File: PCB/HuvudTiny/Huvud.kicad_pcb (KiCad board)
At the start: 4 copper layers, 42 x 42 mm, 98 parts, among them J10 JST_PH, J12 USB_Micro-B_Molex-105017-0001, J2 DBG, J3 THERM, J4 FAN0, J5 FAN1, J6 Heater, J7 Endstop, J8 Conn_01x02, J9 STEPPER, Q1 AO3400A, Q2 AO3400A, Q3 AO3400A, U1 TPS54331DR, U2 TMC2209-LA, U5 STM32F103C8T6, U6 SN65HVD230, Y1 8Mhz

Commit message: v0.44, v0.45
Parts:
- removed C26: 0.1uF, Capacitor_SMD:C_0402_1005Metric
- removed D7: B5819W, Diode_SMD:D_SOD-123
- removed J8: Conn_01x02, Connector_Molex:Molex_Micro-Fit_3.0_43650-0200_1x02_P3.00mm_Horizontal
- removed L2: 22uH, Inductor_SMD:L_0805_2012Metric
- removed L3: 10uH, Inductor_SMD:L_Sunlord_MWSA0518_5.4x5.2mm
- removed R32: 160k, Resistor_SMD:R_0402_1005Metric
- removed R33: 33k, Resistor_SMD:R_0402_1005Metric
- removed U1: TPS54331DR, Package_SO:SOIC-8_3.9x4.9mm_P1.27mm
- added 3.3: TestPoint, TestPoint:TestPoint_Pad_D1.0mm, B.Cu at (198.6, 125.2)
- added C32: 10uF, Capacitor_SMD:C_0805_2012Metric, F.Cu at (196.8, 113.5)
- added GND1: TestPoint, TestPoint:TestPoint_Pad_D1.0mm, B.Cu at (200.9, 125.2)
- added GND2: TestPoint, TestPoint:TestPoint_Pad_D1.0mm, B.Cu at (202.5, 137.2)
- added J1: Conn_02x02_Odd_Even, Connector_Molex:Molex_Micro-Fit_3.0_43045-0400_2x02_P3.00mm_Horizontal, F.Cu at (208.5, 108.5)
- added L4: 10uH/max 145mOhm 2A, Inductor_SMD:L_Sunlord_MWSA0518_5.4x5.2mm, F.Cu at (201.8, 115.2)
- added NT1: Net-Tie_2, NetTie:NetTie-2_SMD_Pad0.5mm, F.Cu at (189.4, 126.3)
- added PB10: TestPoint, TestPoint:TestPoint_Pad_D1.0mm, B.Cu at (198.6, 127.5)
- added PB11: TestPoint, TestPoint:TestPoint_Pad_D1.0mm, B.Cu at (200.8, 127.5)
- added R37: 10k, Resistor_SMD:R_0402_1005Metric, F.Cu at (189.2, 116.2)
- added R38: 100k, Resistor_SMD:R_0402_1005Metric, F.Cu at (213.8, 112.5)
- added R39: 22k, Resistor_SMD:R_0402_1005Metric, F.Cu at (213.4, 113.5)
- added R40: 100k, Resistor_SMD:R_0402_1005Metric, F.Cu at (212.9, 116.8)
- added R41: 22k, Resistor_SMD:R_0402_1005Metric, F.Cu at (213.4, 114.4)
- added TP1: TestPoint, TestPoint:TestPoint_Pad_D1.0mm, B.Cu at (186.4, 118.5)
- added TP2: TestPoint, TestPoint:TestPoint_Pad_D1.0mm, B.Cu at (217.9, 129.4)
- added TP3: TestPoint, TestPoint:TestPoint_Pad_D1.0mm, B.Cu at (217.9, 127.0)
- added TP4: TestPoint, TestPoint:TestPoint_Pad_D1.0mm, B.Cu at (217.9, 124.5)
- added TP5: TestPoint, TestPoint:TestPoint_Pad_D1.0mm, B.Cu at (217.9, 122.0)
- added TP6: TestPoint, TestPoint:TestPoint_Pad_D1.0mm, B.Cu at (183.8, 118.5)
- added U3: TPS54308, Package_TO_SOT_SMD:SOT-23-6, F.Cu at (210.5, 114.9)
- added VIN1: TestPoint, TestPoint:TestPoint_Pad_D1.0mm, B.Cu at (202.5, 139.5)
- C14: value 2.2nF -> 10uF; footprint Capacitor_SMD:C_0402_1005Metric -> Capacitor_SMD:C_0805_2012Metric
- C15: value 22pF/35V -> 10uF; footprint Capacitor_SMD:C_0402_1005Metric -> Capacitor_SMD:C_0805_2012Metric
- C16: value 22nf/50V -> 0.1uF/35V
- C20: value 10uF/35V -> 0.1uF/35V; footprint Capacitor_SMD:C_1206_3216Metric -> Capacitor_SMD:C_0603_1608Metric
- C21: value 0.1uF -> 68pF
- C22: value 10uF -> 10uF/35V; footprint Capacitor_SMD:C_0603_1608Metric -> Capacitor_SMD:C_1210_3225Metric
- C23: value 10uF -> 4.7uF; footprint Capacitor_SMD:C_0603_1608Metric -> Capacitor_SMD:C_0402_1005Metric
- C3, C6, C7: value 0.1uF -> 0.1uF/35V
- D5: value LEDRED -> LEDGR; footprint LED_SMD:LED_0603_1608Metric -> LED_SMD:LED_0402_1005Metric
- H1, H2, H3, H4: footprint MountingHole:MountingHole_3.2mm_M3_Pad -> MountingHole:MountingHole_3.2mm_M3_Pad_Via
- Q3: value AO3400A -> AON7524; footprint Package_TO_SOT_SMD:SOT-23 -> Huvud:DFN-8-1EP_3x3mm_P0.65mm_EP1.7x2.05mm
- R17, R18, R24: value 20k -> 22k
- R2, R29: value 4.7k -> 2.2k
- R27: value 1.5k -> 2.2k
- R30: value 10k -> 22
- R31: value 3.3k -> 22
- R4, R7: value 0.110 -> 0.110 1%
- moved C23 16.4 mm to (191.9, 126.8)
- moved C14 10.7 mm to (196.8, 115.5), turned to 180 degrees
- moved C15 10.5 mm to (196.8, 117.5)
- moved R31 9.98 mm to (211.4, 117.2), turned to 180 degrees
- moved R29 9.73 mm to (213.9, 116.8), turned to 270 degrees
- moved R30 8.25 mm to (207.9, 119.2), turned to 0 degrees
- moved J9 7.70 mm to (220.0, 129.5), turned to 90 degrees
- moved R11 7.66 mm to (200.2, 111.6), turned to 180 degrees
- moved C20 7.63 mm to (205.8, 111.6), turned to 0 degrees
- moved D6 7.05 mm to (202.8, 111.6)
- moved C16 6.83 mm to (206.8, 118.0), turned to 0 degrees
- moved C21 6.28 mm to (213.4, 115.3)
- moved C22 5.92 mm to (206.9, 114.9)
- moved R12 5.12 mm to (204.2, 130.3), turned to 180 degrees
- moved C25 4.98 mm to (193.3, 129.2), turned to 180 degrees
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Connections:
- net /CANH renamed CANH
- net /CANL renamed CANL
- C11 pad 1: GND -> GNDA
- C11 pad 2: +3V3 -> AREF
- C14 pad 1: Net-(C14-Pad1) -> +3V3
- C15 pad 1: GND -> +3V3
- C15 pad 2: Net-(C15-Pad2) -> GND
- C16 pad 1: GND -> ST_VS
- C16 pad 2: Net-(C16-Pad2) -> GND
- C20 pad 1: GND -> Net-(C20-Pad1)
- C20 pad 2: ST_VS -> Net-(C20-Pad2)
- C22 pad 2: +3V3 -> ST_VS
- C23 pad 1: GND -> GNDA
- C23 pad 2: +3V3 -> AREF
- J2 pad 1: BOOT0 -> BOOT1
- J9 pad 1: /ST_B2 -> /ST_A2
- J9 pad 2: /ST_B1 -> /ST_A1
- J9 pad 3: /ST_A1 -> /ST_B1
- J9 pad 4: /ST_A2 -> /ST_B2
- Q3 pad 1: Net-(Q3-Pad1) -> GND
- Q3 pad 2: GND -> Net-(Q3-Pad2)
- R28 pad 2: Net-(Q3-Pad1) -> Net-(Q3-Pad2)
- R29 pad 1: Net-(C14-Pad1) -> Net-(C21-Pad2)
- R29 pad 2: Net-(C15-Pad2) -> Net-(R29-Pad2)
- R30 pad 1: Net-(R30-Pad1) -> +3V3
- R30 pad 2: +3V3 -> Net-(R30-Pad2)
- R31 pad 1: GND -> Net-(R29-Pad2)
- R31 pad 2: Net-(R30-Pad1) -> Net-(R30-Pad2)
- U5 pad 20: (no net) -> BOOT1
- U5 pad 21: (no net) -> Net-(PB10-Pad1)
- U5 pad 22: (no net) -> Net-(PB11-Pad1)
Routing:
- net ST_VS: track 41.7 -> 74.0 mm, vias 15 -> 24
- net BOOT1: track 0.00 -> 23.3 mm, vias 0 -> 1
- net GND: track 142.6 -> 164.3 mm, vias 95 -> 100
- net GNDA: track 11.7 -> 30.4 mm, vias 4 -> 3
- net +3V3: track 45.2 -> 62.5 mm, vias 17 -> 14
- net Net-(C20-Pad1): track 0.00 -> 11.5 mm, vias 0 -> 2
- net CANH: track 10.6 -> 21.3 mm
- net Net-(C20-Pad2): track 0.00 -> 9.12 mm, vias 0 -> 2
- net Net-(C21-Pad1): track 12.7 -> 4.07 mm
- net CANL: track 10.3 -> 17.1 mm
- net LED0: track 14.9 -> 9.30 mm
- net Net-(C15-Pad2): track 5.33 -> 0.00 mm
- net Net-(D3-Pad1): track 11.6 -> 16.8 mm
- net THERM: track 8.65 -> 3.76 mm
- net AREF: track 8.77 -> 12.7 mm
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- added copper zone on In1.Cu, net GNDA
- added copper zone on F.Cu, net Net-(D3-Pad1)
- removed copper zone on B.Cu, net GNDA
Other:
- board text added: "B0"
- board text added: "GND"
- board text added: "GND VIN"
- board text added: "HUVUD"
- board text added: "IO RST B1"
- board text added: "v0.45"
- board text removed: "3.3V"
- board text removed: "IO RST B0"
- board text removed: "v0.41"
- board text removed: "µHUVUD"

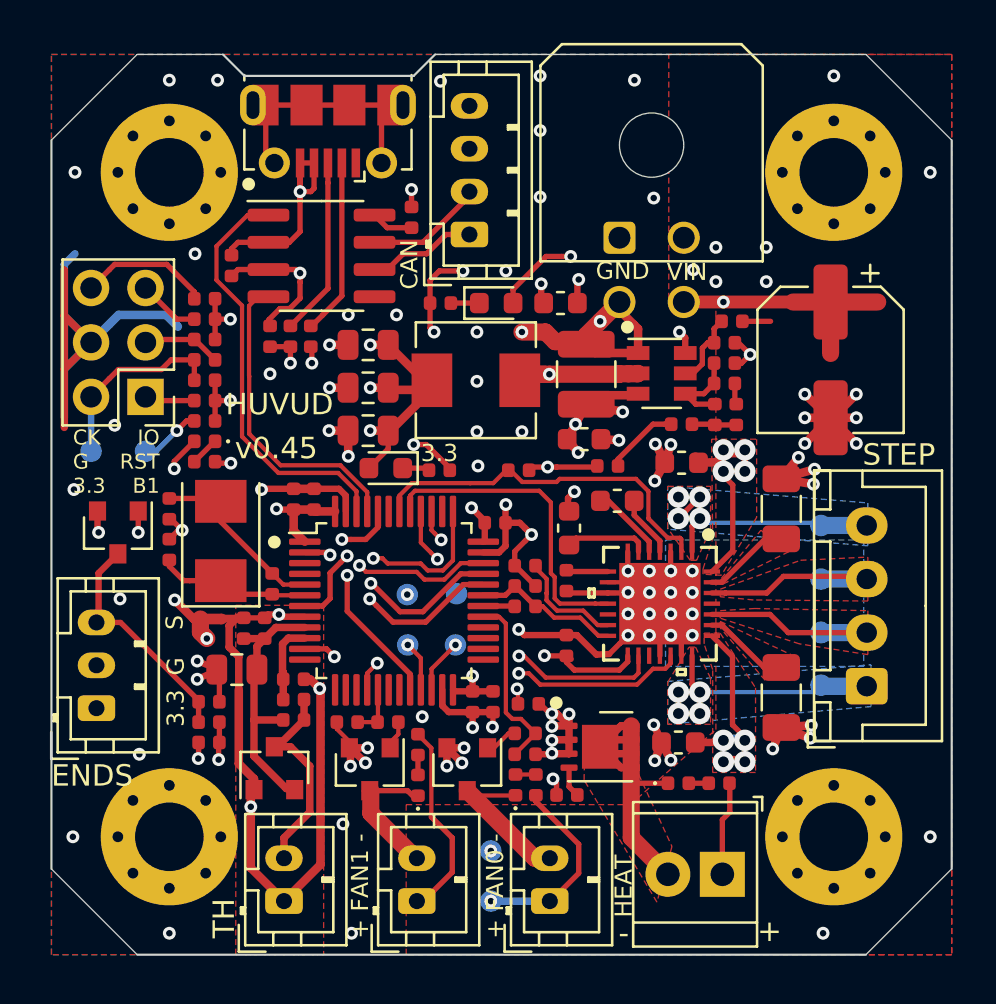
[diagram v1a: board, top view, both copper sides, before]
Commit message: Minor tweaks to the layout. Added some text on the back size
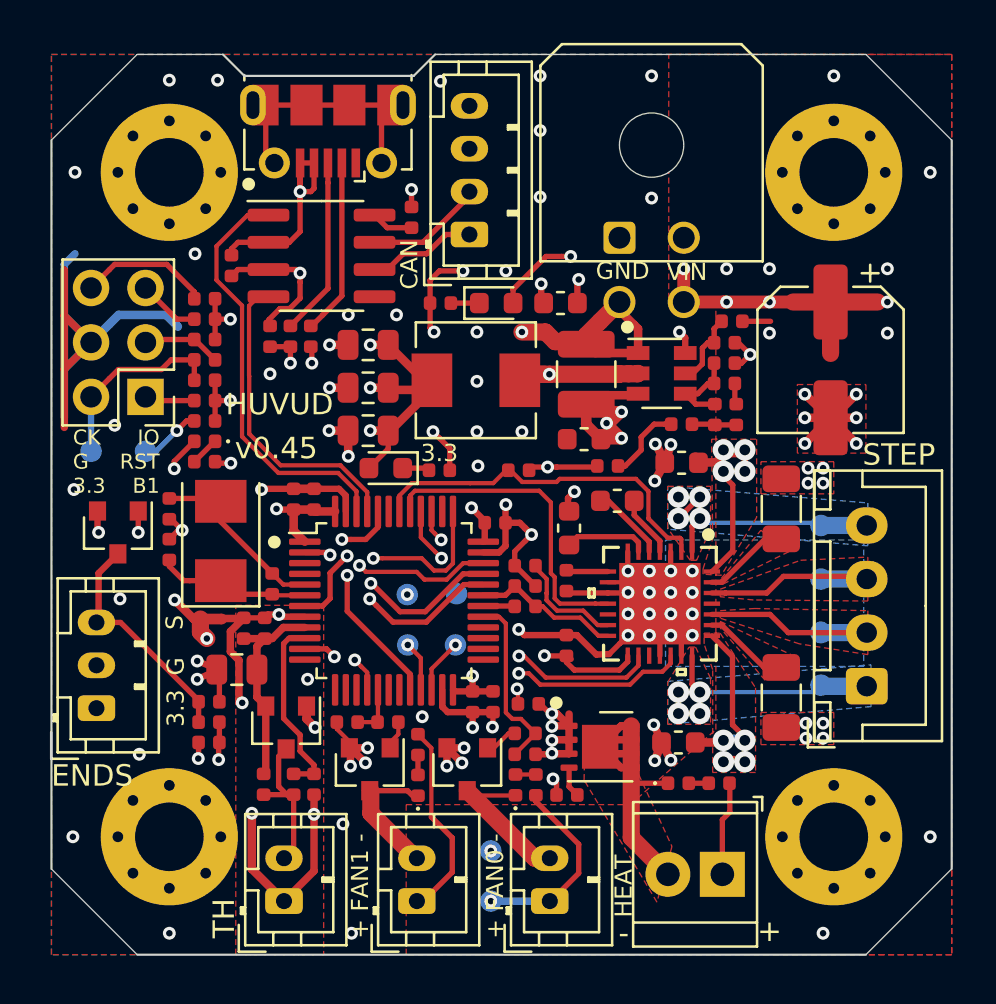
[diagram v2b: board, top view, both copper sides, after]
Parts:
- added REF**: OSHW-Logo_7.5x8mm_SilkScreen, Symbol:OSHW-Logo_7.5x8mm_SilkScreen, B.Cu at (194.8, 109.8)
- moved C25 4.99 mm to (194.2, 134.1), turned to 90 degrees
- moved R5 3.95 mm to (193.3, 134.1), turned to 270 degrees
- moved R2 3.31 mm to (191.9, 134.1), turned to 90 degrees
- moved D9 1.98 mm to (192.9, 131.4), turned to 270 degrees
- turned C16 to 180 degrees
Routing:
- net GNDA: track 30.4 -> 19.9 mm, vias 3 -> 6
- net GND: track 164.3 -> 155.0 mm, vias 100 -> 99
- net ST_VS: track 74.0 -> 79.5 mm, vias 24 -> 27
- net THERM: track 3.76 -> 8.71 mm
- net AREF: track 12.7 -> 9.74 mm
- net Net-(D9-Pad3): track 9.67 -> 7.31 mm
- net HEATER: track 15.3 -> 16.7 mm
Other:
- board text added: "github.com/bondus/KlipperToolboard"
